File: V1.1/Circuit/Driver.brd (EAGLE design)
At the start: 160 x 100 mm, 25 parts, among them IC1 DRV8300DIPWR

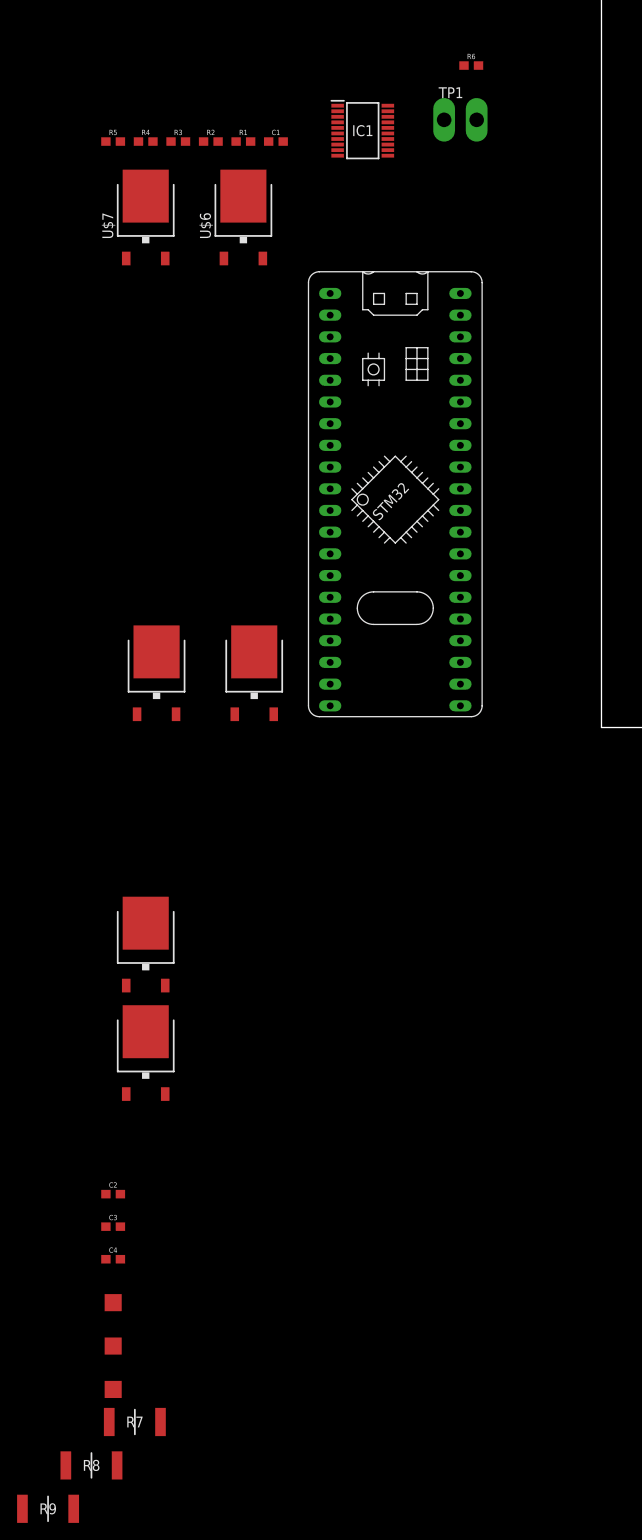
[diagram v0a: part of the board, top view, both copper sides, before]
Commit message: Added the FOC library
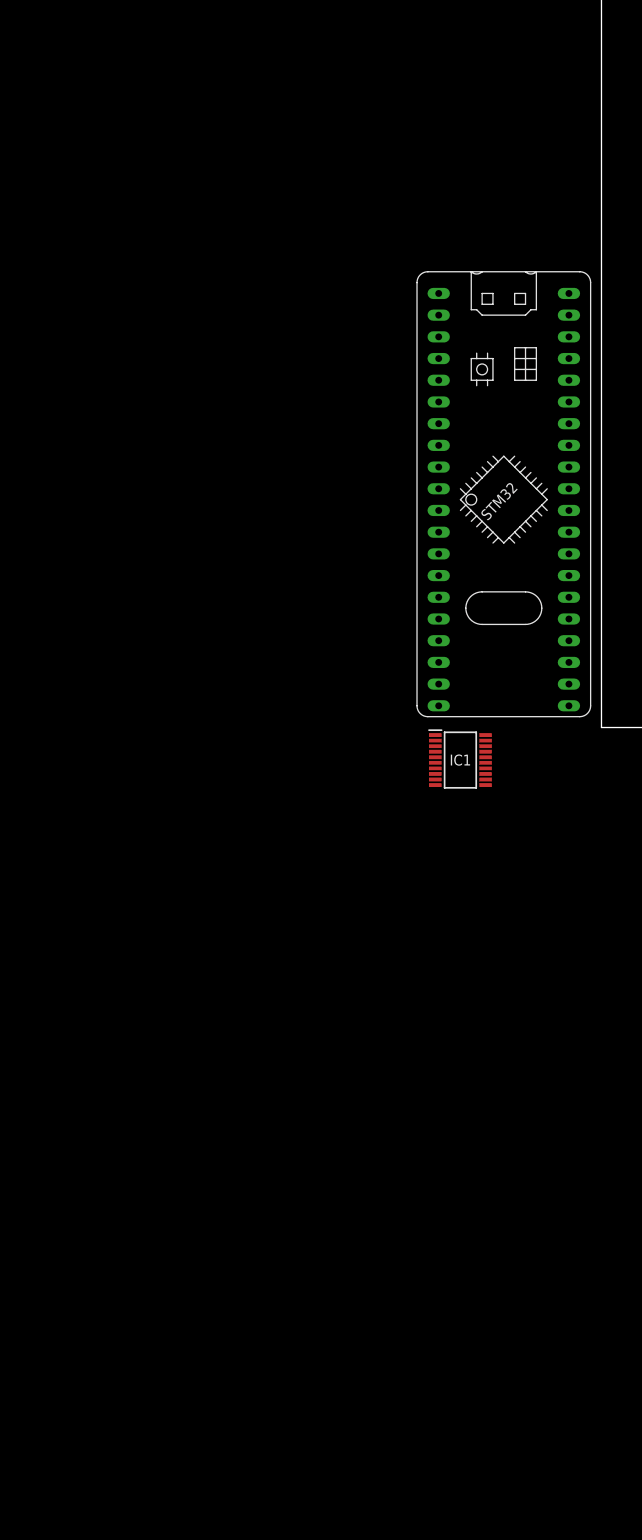
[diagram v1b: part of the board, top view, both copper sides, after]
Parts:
- removed C1: 10uF, SparkFun-Capacitors:0603
- removed C2, C3, C4: 1.0uF, SparkFun-Capacitors:0603
- removed R1, R2, R3, R4, R5, R6: 100, SparkFun-Resistors:0603
- removed R7, R8, R9: CR2512-FX-51R1ELF, CR2512-FX-51R1ELF:RESC6331X75N
- removed TP1: PTR2, testpad:P2-38-17
- removed TP2, TP3, TP4: TPTP20SQ, testpad:TP20SQ
- removed U$2, U$3, U$4, U$5, U$6, U$7: IRLR7843, BLDC project:TO252
- moved IC1 74.5 mm to (-16.5, -3.81)
- moved U$1 12.7 mm to (-11.4, 35.6)
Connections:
- removed net BSTA: C2.2, IC1.20
- removed net BSTB: C3.2, IC1.17
- removed net BSTC: C4.2, IC1.14
- removed net GHA: IC1.19, R1.1
- removed net GHB: IC1.16, R2.1
- removed net GHC: IC1.13, R3.1
- removed net GLA: IC1.11
- removed net GLB: IC1.10
- removed net GLC: IC1.9
- removed net INHA: IC1.1
- removed net INHB: IC1.2
- removed net INHC: IC1.3
- removed net INLA: IC1.4
- removed net INLB: IC1.5
- removed net INLC: IC1.6
- removed net N$1: R1.2, U$2.1
- removed net N$2: R2.2, U$4.1
- removed net N$3: R3.2, U$6.1
- removed net N$4: R5.2, U$3.1
- removed net N$5: R6.2, U$5.1
- removed net N$6: R4.2, U$7.1
- removed net N$7: R7.1, TP2.TP
- removed net N$8: R8.1, TP3.TP
- removed net N$9: R9.1, TP4.TP
- removed net SHA: C2.1, IC1.18, R5.1, R7.2, U$2.2, U$3.3
- removed net SHB: C3.1, IC1.15, R6.1, R8.2, U$4.2, U$5.3
- removed net SHC: C4.1, IC1.12, R4.1, R9.2, U$6.2, U$7.3
- removed net VCC: C1.1, IC1.7, TP1.TP-1, U$2.3, U$4.3, U$6.3
- net GND: no longer C1.2, IC1.8, TP1.TP-2, U$3.2, U$5.2, U$7.2

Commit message: Circuit: Added DRV8300, and the Gate Circuit. Haven't added the Not gate
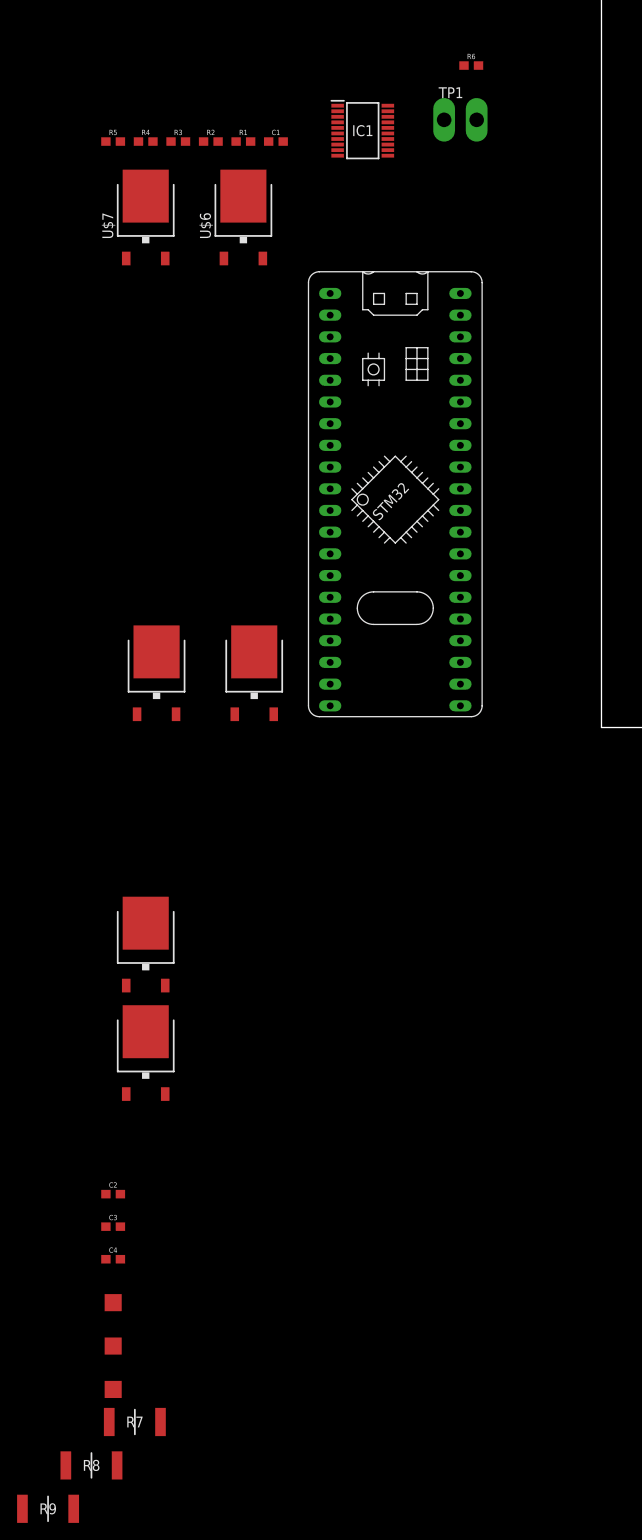
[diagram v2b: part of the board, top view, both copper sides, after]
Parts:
- added C1: 10uF, SparkFun-Capacitors:0603
- added C2, C3, C4: 1.0uF, SparkFun-Capacitors:0603
- added R1, R2, R3, R4, R5, R6: 100, SparkFun-Resistors:0603
- added R7, R8, R9: CR2512-FX-51R1ELF, CR2512-FX-51R1ELF:RESC6331X75N
- added TP1: PTR2, testpad:P2-38-17
- added TP2, TP3, TP4: TPTP20SQ, testpad:TP20SQ
- added U$2, U$3, U$4, U$5, U$6, U$7: IRLR7843, BLDC project:TO252
- moved IC1 74.5 mm to (-27.9, 69.8)
- moved U$1 12.7 mm to (-24.1, 35.6)
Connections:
- new net BSTA: C2.2, IC1.20
- new net BSTB: C3.2, IC1.17
- new net BSTC: C4.2, IC1.14
- new net GHA: IC1.19, R1.1
- new net GHB: IC1.16, R2.1
- new net GHC: IC1.13, R3.1
- new net GLA: IC1.11
- new net GLB: IC1.10
- new net GLC: IC1.9
- new net INHA: IC1.1
- new net INHB: IC1.2
- new net INHC: IC1.3
- new net INLA: IC1.4
- new net INLB: IC1.5
- new net INLC: IC1.6
- new net N$1: R1.2, U$2.1
- new net N$2: R2.2, U$4.1
- new net N$3: R3.2, U$6.1
- new net N$4: R5.2, U$3.1
- new net N$5: R6.2, U$5.1
- new net N$6: R4.2, U$7.1
- new net N$7: R7.1, TP2.TP
- new net N$8: R8.1, TP3.TP
- new net N$9: R9.1, TP4.TP
- new net SHA: C2.1, IC1.18, R5.1, R7.2, U$2.2, U$3.3
- new net SHB: C3.1, IC1.15, R6.1, R8.2, U$4.2, U$5.3
- new net SHC: C4.1, IC1.12, R4.1, R9.2, U$6.2, U$7.3
- new net VCC: C1.1, IC1.7, TP1.TP-1, U$2.3, U$4.3, U$6.3
- net GND: now also C1.2, IC1.8, TP1.TP-2, U$3.2, U$5.2, U$7.2
